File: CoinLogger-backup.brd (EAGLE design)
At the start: 27.9 x 27.9 mm, 18 parts, among them IC1 TINY11S, U4 LIS331, X1 USB-MICROB

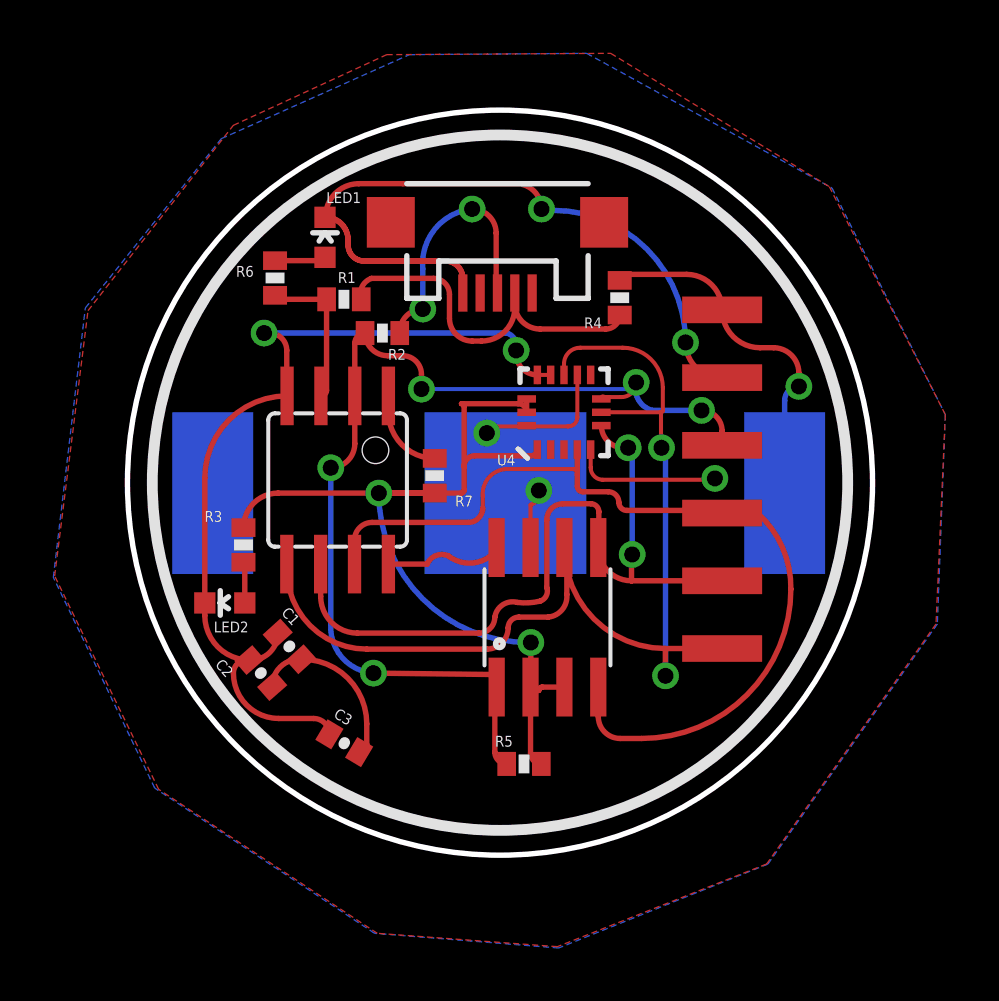
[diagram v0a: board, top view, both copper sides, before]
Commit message: Updated and rerouted V1.1, early nanologger layout
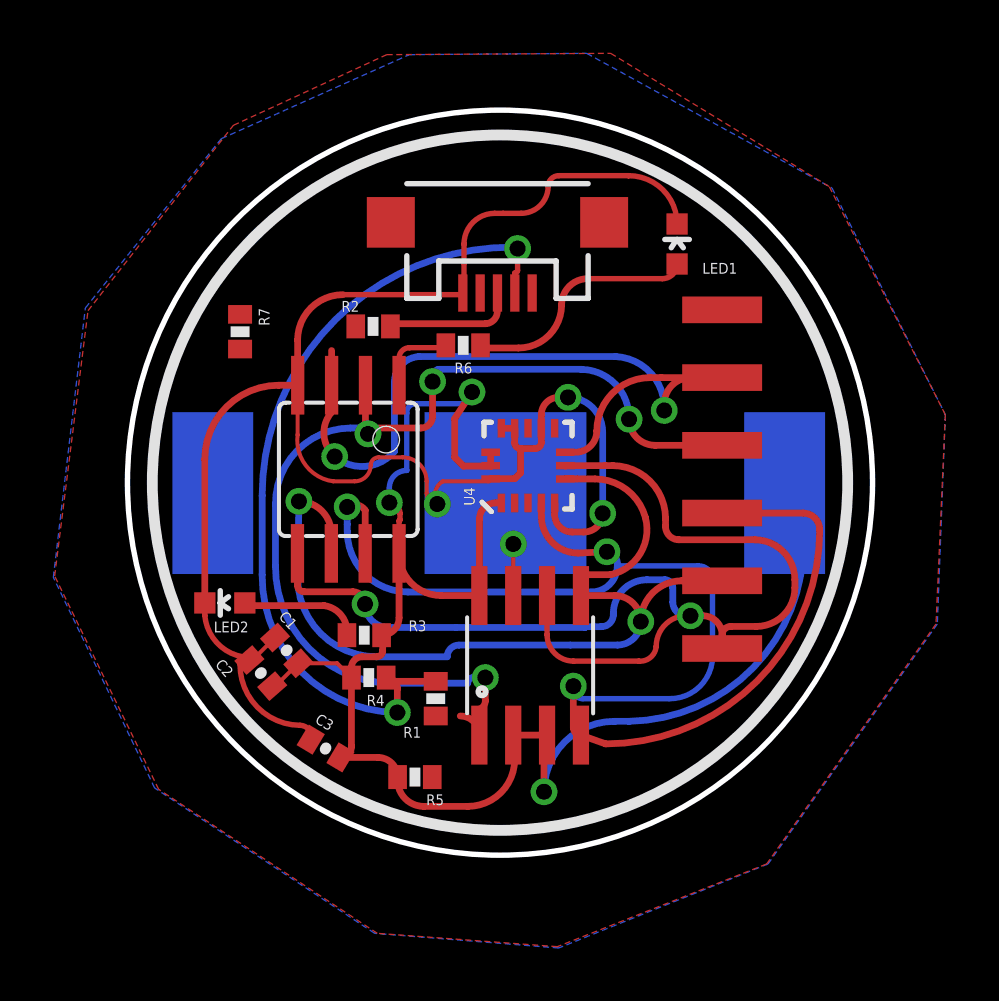
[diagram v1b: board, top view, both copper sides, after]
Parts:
- moved R4 17.1 mm to (17.1, 29.7), turned to 180 degrees
- moved R1 15.4 mm to (19.6, 28.9), turned to 90 degrees
- moved LED1 13.2 mm to (28.6, 46.0)
- moved R7 9.08 mm to (12.3, 42.7)
- moved R6 7.49 mm to (20.6, 42.2), turned to 180 degrees
- moved R3 5.65 mm to (16.9, 31.3), turned to 0 degrees
- moved R5 4.12 mm to (18.8, 26.0), turned to 180 degrees
- moved U4 2.41 mm to (23.1, 37.6)
- moved U$1 1.91 mm to (23.1, 30.1)
- moved C3 0.73 mm to (15.5, 27.0)
- moved IC1 0.57 mm to (16.3, 37.5)
- moved R2 0.43 mm to (17.2, 42.9)
- moved C1 0.18 mm to (14.0, 30.7)
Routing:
- net N$13: track 5.70 -> 27.4 mm, vias 0 -> 2
- net N$5: track 33.4 -> 49.9 mm, vias 0 -> 3
- net N$8: track 13.8 -> 28.8 mm, vias 0 -> 2
- net GND: track 83.1 -> 72.5 mm, vias 7 -> 4
- net N$10: track 1.92 -> 8.72 mm
- net N$7: track 28.8 -> 34.5 mm
- net N$2: track 9.24 -> 4.93 mm, vias 2 -> 0
- net VCC: track 57.9 -> 62.0 mm
- net N$3: track 1.54 -> 4.42 mm
- net N$6: track 41.3 -> 43.1 mm
- net N$4: track 40.4 -> 38.6 mm, vias 5 -> 4
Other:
- board text added: "01/04/14"
- board text removed: "01/07/14"
